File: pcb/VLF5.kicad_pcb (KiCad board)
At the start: 6 copper layers, 34 x 56 mm, 92 parts, among them CN1 532610571, J1 Conn_01x02_Pin, Q1 SS8050, Q3 SS8050, Q4 SS8050, Q5 SI7232DN-T1-GE3, U1 STM32H743VIHx, U10 LSM6DSMTR, U11 LIS2MDL, U15 ISO1044BD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

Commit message: ufl
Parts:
- added R14: 0R, Resistor_SMD:R_0603_1608Metric, B.Cu at (91.4, 7.57)
- added U8: BWU.FL-IPEX1, Rocketry_Easyeda:IPEX-SMD_BWIPX-1-001E, B.Cu at (83.5, 9.34)
- moved U6 1.65 mm to (83.7, 2.13)

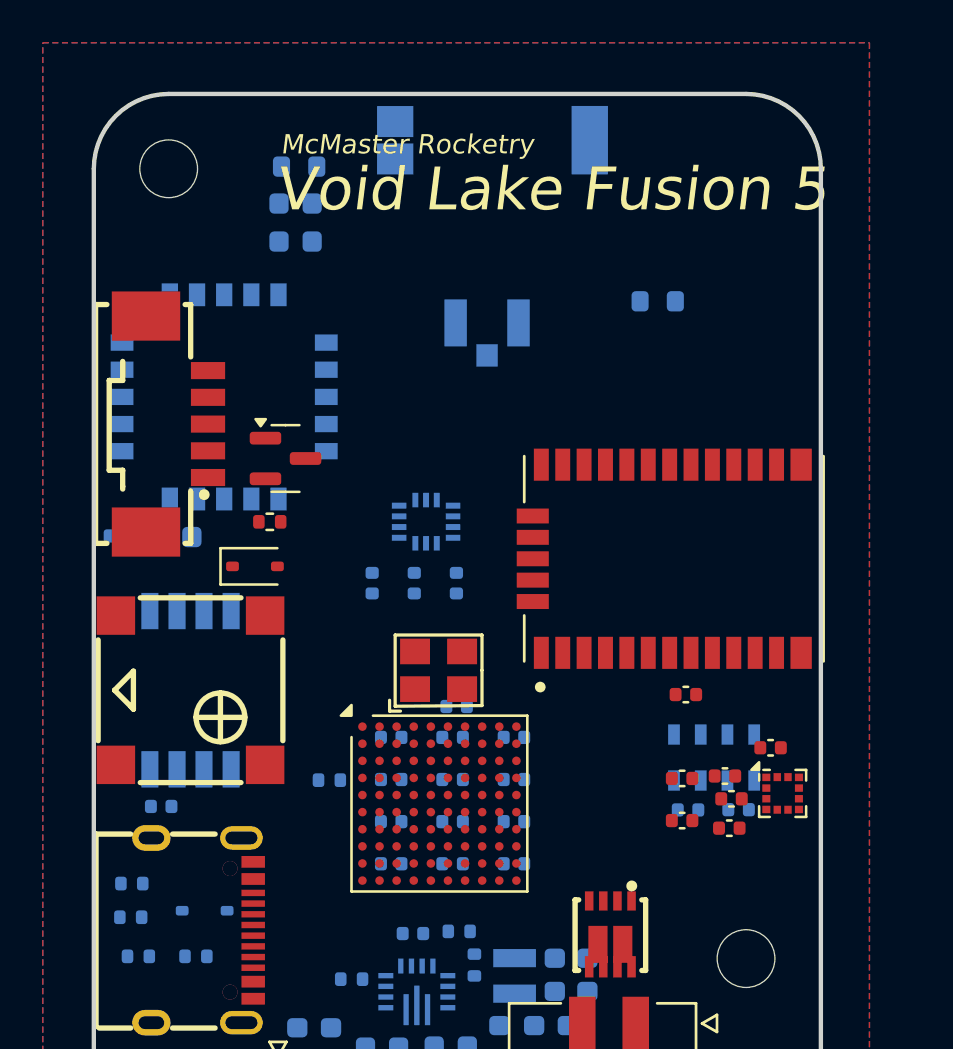
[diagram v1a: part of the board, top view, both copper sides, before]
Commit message: added active gps antenna connector
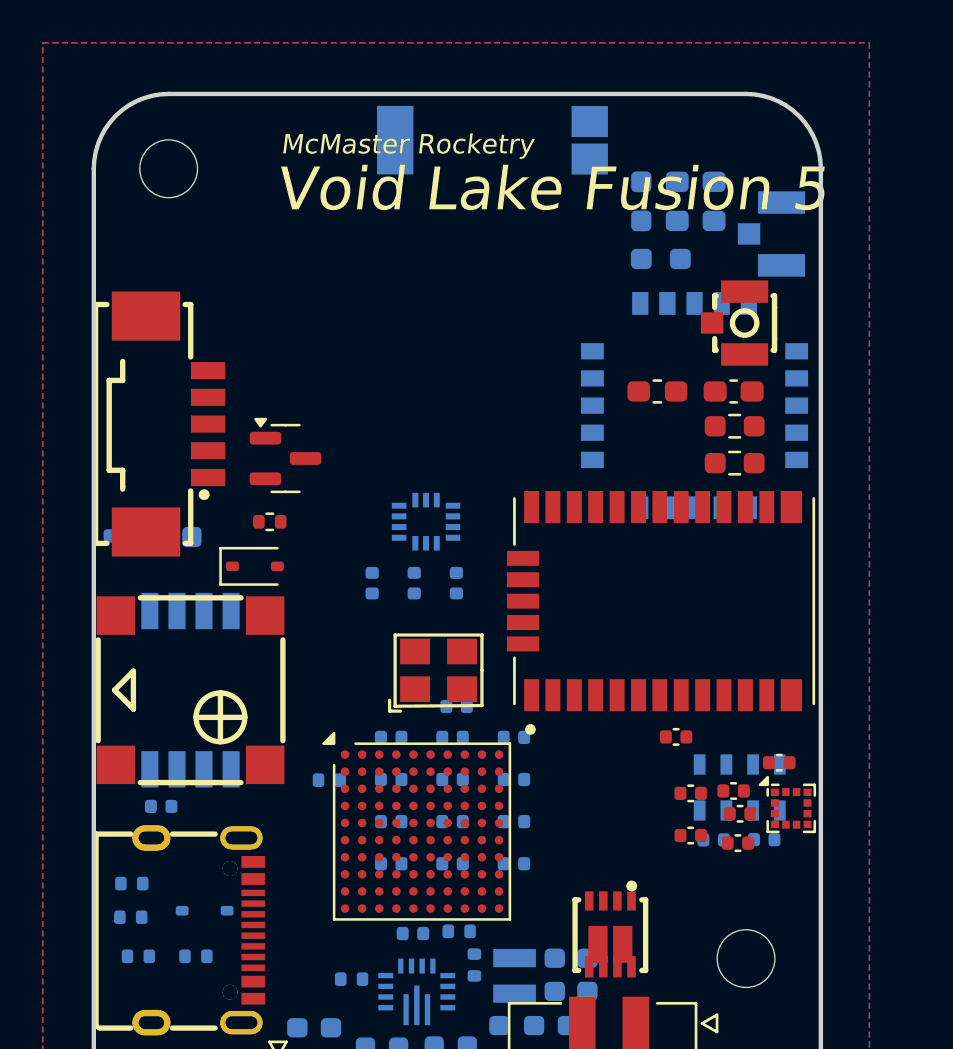
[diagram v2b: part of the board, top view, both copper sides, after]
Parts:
- added C13: 47pF, Capacitor_SMD:C_0603_1608Metric_Pad1.08x0.95mm_HandSolder, F.Cu at (95.0, 11.8)
- added L3: 27nH, Inductor_SMD:L_0603_1608Metric_Pad1.05x0.95mm_HandSolder, F.Cu at (91.4, 11.8)
- added R16: 0R, Resistor_SMD:R_0603_1608Metric_Pad0.98x0.95mm_HandSolder, F.Cu at (95.0, 13.4)
- added R17: 0R, Resistor_SMD:R_0603_1608Metric_Pad0.98x0.95mm_HandSolder, F.Cu at (95.0, 15.1)
- added U12: BWU.FL-IPEX1, Rocketry_Easyeda:IPEX-SMD_BWIPX-1-001E, F.Cu at (94.8, 8.59)
- C28, C46: footprint Capacitor_SMD:C_0603_1608Metric -> Capacitor_SMD:C_0603_1608Metric_Pad1.08x0.95mm_HandSolder
- R14, R31: footprint Resistor_SMD:R_0603_1608Metric -> Resistor_SMD:R_0603_1608Metric_Pad0.98x0.95mm_HandSolder
- U6: footprint Rocketry_Manual:W3012-ANT-PKG-Mirrored -> Rocketry_Manual:W3012-ANT-PKG
- moved U7 22.0 mm to (93.2, 12.4)
- moved C46 18.9 mm to (93.2, 1.98), turned to 0 degrees
- moved C28 18.7 mm to (93.2, 3.81), turned to 0 degrees
- moved R31 16.1 mm to (90.7, 2.90), turned to -90 degrees
- moved U8 13.9 mm to (96.5, 4.42), turned to 0 degrees
- moved C27 2.03 mm to (92.3, 27.9)
- moved U5 2.03 mm to (91.7, 21.6)
- moved R14 1.99 mm to (91.6, 5.59)
- moved C12 1.84 mm to (96.4, 32.7)
- moved U9 1.84 mm to (95.3, 30.3)
- moved C11 1.84 mm to (94.1, 32.8)
- moved U1 1.54 mm to (80.4, 32.4)
- moved C22 0.81 mm to (95.0, 30.5)
- moved C23 0.81 mm to (95.3, 31.5)
- moved C24 0.81 mm to (95.2, 32.9)
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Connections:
- C23 pad 2: +3.3VA -> +3.3V
- C24 pad 2: +3.3VA -> +3.3V
- C41 pad 2: +3.3VA -> +3.3V
- R14 pad 2: Net-(U6-ANT) -> Net-(U7-ANT)
- U11 pad 10: +3.3VA -> +3.3V
- U5 pad 16: Net-(U5-RF_IN) -> Net-(U5-RF_OUT)

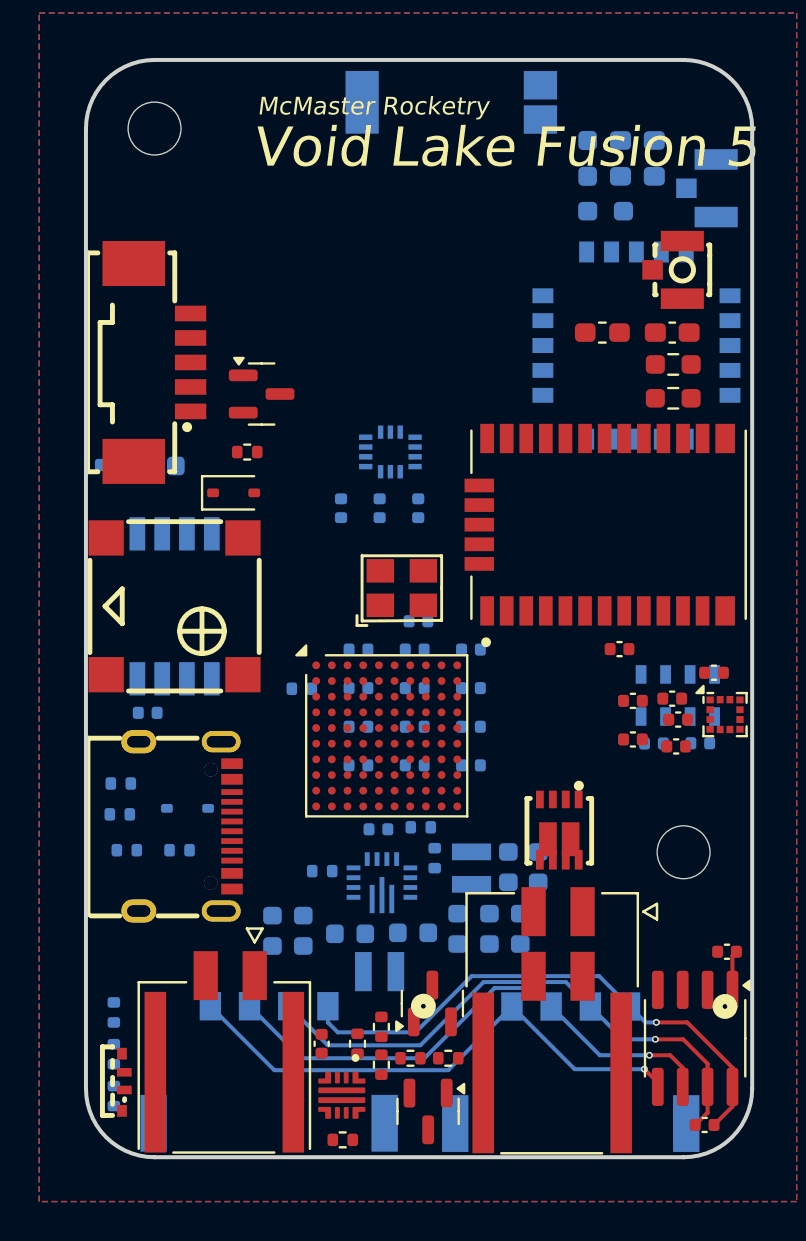
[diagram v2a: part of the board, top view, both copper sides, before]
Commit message: add pull up resistor for sd, change pad net
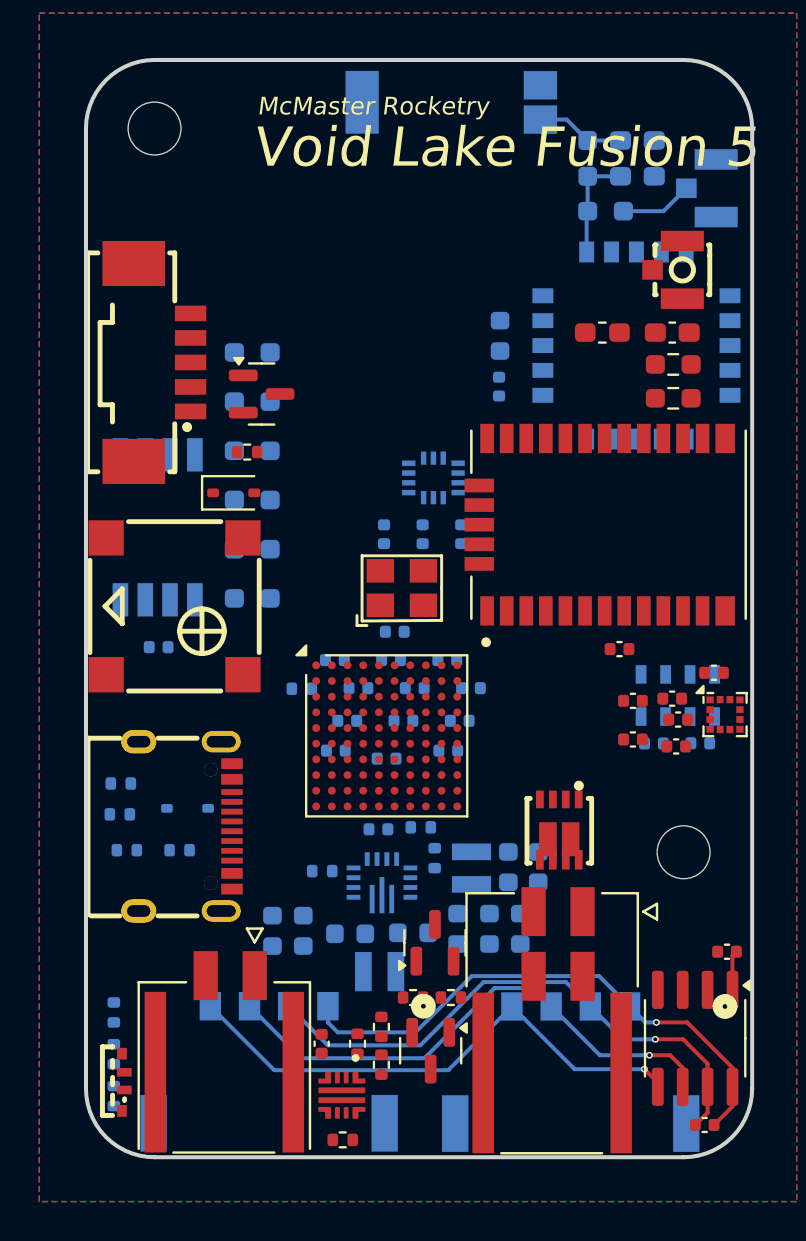
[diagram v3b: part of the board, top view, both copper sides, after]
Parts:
- added R15: 10K, Resistor_SMD:R_0603_1608Metric_Pad0.98x0.95mm_HandSolder, B.Cu at (73.6, 12.8)
- added R18: 10K, Resistor_SMD:R_0603_1608Metric_Pad0.98x0.95mm_HandSolder, B.Cu at (73.6, 15.3)
- added R19: 10K, Resistor_SMD:R_0603_1608Metric_Pad0.98x0.95mm_HandSolder, B.Cu at (73.6, 17.8)
- added R20: 10K, Resistor_SMD:R_0603_1608Metric_Pad0.98x0.95mm_HandSolder, B.Cu at (73.6, 20.3)
- added R21: 10K, Resistor_SMD:R_0603_1608Metric_Pad0.98x0.95mm_HandSolder, B.Cu at (73.6, 22.8)
- added R23: 10K, Resistor_SMD:R_0603_1608Metric_Pad0.98x0.95mm_HandSolder, B.Cu at (73.6, 25.3)
- moved C25 20.3 mm to (86.2, 14.5), turned to -90 degrees
- moved C26 18.6 mm to (86.2, 12.0), turned to -90 degrees
- moved U2 4.12 mm to (68.7, 21.7)
- moved C20 3.40 mm to (68.8, 27.8)
- moved R10 3.10 mm to (81.8, 45.7)
- moved Q3 3.10 mm to (82.7, 48.4)
- moved R9 3.10 mm to (83.7, 45.7)
- moved Q1 3.10 mm to (82.9, 42.9)
- moved C16 2.57 mm to (84.2, 22.1)
- moved C17 2.57 mm to (82.3, 22.1)
- moved C18 2.57 mm to (80.3, 22.1)
- moved U10 2.57 mm to (82.8, 19.2)
- moved C36 1.48 mm to (80.4, 33.5)
- moved C40 1.38 mm to (77.8, 33.1)
- moved C32 1.38 mm to (83.6, 33.1)
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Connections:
- net /Peripherals/IMU_INT1 renamed /IMU_INT1
- net /Peripherals/IMU_INT2 renamed /IMU_INT2
- net /Pyro/PYRO1_CONT renamed /PYRO1_CONT
- net /Pyro/PYRO2_CONT renamed /PYRO2_CONT
- net /RF/GPS_PPS renamed /GPS_PPS
- J1 pad S2: (no net) -> +BATT
- J_PYRO1 pad S1: (no net) -> Net-(J_PYRO1-Pin_3)
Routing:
- net Net-(U7-ANT): track 0.00 -> 5.56 mm
- net Net-(U6-ANT): track 0.00 -> 4.53 mm
- net Net-(R14-Pad1): track 0.00 -> 3.70 mm

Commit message: Original Layout with Pins Configured
🙏
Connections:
- D1 pad 2: /Power/VBUS -> /VBUS
- J1 pad S2: +BATT -> (no net)
- J_PYRO1 pad S1: Net-(J_PYRO1-Pin_3) -> (no net)
- Q5 pad 2: /Pyro/PYRO1_CTRL -> /PYRO1_CTRL
- Q5 pad 4: /Pyro/PYRO2_CTRL -> /PYRO2_CTRL
- R11 pad 1: /Power/BAT_V_M -> /BAT_V_M
- R12 pad 2: /Power/BAT_V_M -> /BAT_V_M
- R13 pad 2: /Peripherals/BUZZER_CTRL -> /BUZZER_CTRL
- R15 pad 1: /Peripherals/SD_DAT2 -> /SD_DAT2
- R18 pad 1: /Peripherals/SD_DAT3 -> /SD_DAT3
- R19 pad 1: /Peripherals/SD_CLK -> /SD_CLK
- R20 pad 1: /Peripherals/SD_DAT1 -> /SD_DAT1
- R21 pad 1: /Peripherals/SD_DAT0 -> /SD_DAT0
- R23 pad 1: /Peripherals/SD_CMD -> /SD_CMD
- R24 pad 1: /Peripherals/LED_B_CTRL -> /LED_B_CTRL
- R25 pad 1: /Peripherals/LED_G_CTRL -> /LED_G_CTRL
- R26 pad 1: /Peripherals/LED_R_CTRL -> /LED_R_CTRL
- R8 pad 2: /Pyro/PYRO_nEN -> /PYRO_nEN
- U1 pad A1: unconnected-(U1-PC14-PadA1) -> /IMU_INT1
- U1 pad A2: unconnected-(U1-PC13-PadA2) -> /IMU_CS
- U1 pad A3: unconnected-(U1-PE2-PadA3) -> /IMU_CLK
- U1 pad A4: unconnected-(U1-PB9-PadA4) -> /IMU_INT2
- U1 pad A5: unconnected-(U1-PB7-PadA5) -> /MAG_SDA
- U1 pad A6: unconnected-(U1-PB4-PadA6) -> /LORA_MISO
- U1 pad A7: unconnected-(U1-PB3-PadA7) -> /LORA_SCK
- U1 pad A8: unconnected-(U1-PA15-PadA8) -> /GPS_PPS
- U1 pad B1: unconnected-(U1-PC15-PadB1) -> /BUZZER_CTRL
- U1 pad B10: unconnected-(U1-PA12-PadB10) -> /DP
- U1 pad B4: unconnected-(U1-PB8-PadB4) -> /MAG_SCL
- U1 pad B5: unconnected-(U1-PB6-PadB5) -> /GPS_TX
- U1 pad B6: unconnected-(U1-PD5-PadB6) -> /LORA_nRST
- U1 pad B7: unconnected-(U1-PD2-PadB7) -> /SD_CMD
- U1 pad B8: unconnected-(U1-PC11-PadB8) -> /SD_DAT3
- U1 pad B9: unconnected-(U1-PC10-PadB9) -> /SD_DAT2
- U1 pad C10: unconnected-(U1-PA11-PadC10) -> /DN
- U1 pad C5: unconnected-(U1-PB5-PadC5) -> /BARO_MOSI
- U1 pad C6: unconnected-(U1-PD6-PadC6) -> /LORA_MOSI
- U1 pad C7: unconnected-(U1-PD3-PadC7) -> /LORA_BUSY
- U1 pad C8: unconnected-(U1-PC12-PadC8) -> /SD_CLK
- U1 pad C9: unconnected-(U1-PA9-PadC9) -> /VBUS
- U1 pad D10: unconnected-(U1-PA10-PadD10) -> /GPS_RX
- U1 pad D3: unconnected-(U1-PE5-PadD3) -> /IMU_MISO
- U1 pad D7: unconnected-(U1-PD4-PadD7) -> /LORA_CS
- U1 pad D8: unconnected-(U1-PD0-PadD8) -> /LORA_RXEN
- U1 pad D9: unconnected-(U1-PA8-PadD9) -> /LORA_DIO1
- U1 pad E10: unconnected-(U1-PC7-PadE10) -> /GPS_nRST
- U1 pad E3: unconnected-(U1-PE6-PadE3) -> /IMU_MOSI
- U1 pad E8: unconnected-(U1-PD1-PadE8) -> /LORA_TXEN
- U1 pad E9: unconnected-(U1-PC9-PadE9) -> /SD_DAT1
- U1 pad F10: unconnected-(U1-PC6-PadF10) -> /BARO_CS
- U1 pad F9: unconnected-(U1-PC8-PadF9) -> /SD_DAT0
- U1 pad G9: unconnected-(U1-PD11-PadG9) -> /PYRO_nEN
- U1 pad H3: unconnected-(U1-PA5-PadH3) -> /BARO_CLK
- U1 pad H9: unconnected-(U1-PD10-PadH9) -> /PYRO_PG
- U1 pad J10: unconnected-(U1-PD13-PadJ10) -> /PYRO1_CONT
- U1 pad J3: unconnected-(U1-PA6-PadJ3) -> /BARO_MISO
- U1 pad J4: unconnected-(U1-PB0-PadJ4) -> /BAT_V_M
- U1 pad J8: unconnected-(U1-PB13-PadJ8) -> /CAN_TX
- U1 pad J9: unconnected-(U1-PD9-PadJ9) -> /PYRO2_CTRL
- U1 pad K10: unconnected-(U1-PD12-PadK10) -> /PYRO2_CONT
- U1 pad K2: unconnected-(U1-PA3-PadK2) -> /LED_R_CTRL
- U1 pad K3: unconnected-(U1-PA7-PadK3) -> /LED_G_CTRL
- U1 pad K4: unconnected-(U1-PB1-PadK4) -> /LED_B_CTRL
- U1 pad K6: unconnected-(U1-PE13-PadK6) -> /PS
- U1 pad K8: unconnected-(U1-PB12-PadK8) -> /CAN_RX
- U1 pad K9: unconnected-(U1-PD8-PadK9) -> /PYRO1_CTRL
- U10 pad 1: /Peripherals/IMU_MISO -> /IMU_MISO
- U10 pad 12: /Peripherals/IMU_CS -> /IMU_CS
- U10 pad 13: /Peripherals/IMU_CLK -> /IMU_CLK
- U10 pad 14: /Peripherals/IMU_MOSI -> /IMU_MOSI
- U11 pad 1: /Peripherals/MAG_SCL -> /MAG_SCL
- U11 pad 4: /Peripherals/MAG_SDA -> /MAG_SDA
- U15 pad 2: /Peripherals/CAN_TX -> /CAN_TX
- U15 pad 3: /Peripherals/CAN_RX -> /CAN_RX
- U2 pad 1: /Peripherals/SD_DAT2 -> /SD_DAT2
- U2 pad 2: /Peripherals/SD_DAT3 -> /SD_DAT3
- U2 pad 3: /Peripherals/SD_CLK -> /SD_CLK
- U2 pad 5: /Peripherals/SD_CMD -> /SD_CMD
- U2 pad 6: /Peripherals/SD_DAT0 -> /SD_DAT0
- U2 pad 7: /Peripherals/SD_DAT1 -> /SD_DAT1
- U3 pad 2: /Pyro/PYRO_nEN -> /PYRO_nEN
- U3 pad 3: /Pyro/PYRO_PG -> /PYRO_PG
- U4 pad 1: /Power/PS -> /PS
- U5 pad 23: /RF/GPS_nRST -> /GPS_nRST
- U5 pad 25: /RF/GPS_TX -> /GPS_TX
- U5 pad 26: /RF/GPS_RX -> /GPS_RX
- U7 pad 10: /RF/LORA_RXEN -> /LORA_RXEN
- U7 pad 11: /RF/LORA_BUSY -> /LORA_BUSY
- U7 pad 12: /RF/LORA_MISO -> /LORA_MISO
- U7 pad 13: /RF/LORA_MOSI -> /LORA_MOSI
- U7 pad 14: /RF/LORA_CS -> /LORA_CS
- U7 pad 15: /RF/LORA_SCK -> /LORA_SCK
- U7 pad 20: /RF/LORA_DIO1 -> /LORA_DIO1
- U7 pad 3: /RF/LORA_nRST -> /LORA_nRST
- U7 pad 9: /RF/LORA_TXEN -> /LORA_TXEN
- U9 pad 4: /Peripherals/BARO_CS -> /BARO_CS
- U9 pad 5: /Peripherals/BARO_CS -> /BARO_CS
- U9 pad 6: /Peripherals/BARO_MISO -> /BARO_MISO
- U9 pad 7: /Peripherals/BARO_MOSI -> /BARO_MOSI
- U9 pad 8: /Peripherals/BARO_CLK -> /BARO_CLK
- USB1 pad 11: /Power/VBUS -> /VBUS
- USB1 pad 2: /Power/VBUS -> /VBUS
- USB1 pad 5: /Power/DN -> /DN
- USB1 pad 6: /Power/DP -> /DP
- USB1 pad 7: /Power/DN -> /DN
- USB1 pad 8: /Power/DP -> /DP
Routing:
- added copper zone on B.Cu, net +3.3V
- added copper zone on B.Cu, net +BATT

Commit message: Playing with configs Template
As title describes
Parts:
- moved C44 77.4 mm to (116.1, 96.0)
- moved C33 77.1 mm to (116.1, 97.0)
- moved RBOOT1 76.8 mm to (109.5, 99.1), turned to -90 degrees
- moved C37 76.5 mm to (114.1, 95.8)
- moved C36 75.7 mm to (116.2, 100.3)
- moved C38 75.7 mm to (114.1, 97.0)
- moved C39 75.5 mm to (114.0, 98.1)
- moved C40 75.3 mm to (114.1, 99.2)
- moved C34 74.1 mm to (108.4, 99.1), turned to -90 degrees
- moved C31 73.8 mm to (116.2, 98.1)
- moved C32 73.7 mm to (116.3, 99.2)
- moved C35 73.6 mm to (110.5, 99.1), turned to -90 degrees
- moved Q5 61.0 mm to (82.7, 97.8)
- moved Q1 57.0 mm to (77.9, 99.7)
- moved R10 55.1 mm to (81.8, 100.8)
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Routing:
- net Net-(J_CAN1-Pin_2): track 28.7 -> 0.00 mm, vias 1 -> 0
- net Net-(J_CAN1-Pin_1): track 28.1 -> 0.00 mm, vias 1 -> 0
- net Net-(J_CAN1-Pin_4): track 27.4 -> 0.00 mm, vias 1 -> 0
- net Net-(J_CAN1-Pin_3): track 27.4 -> 0.00 mm, vias 1 -> 0
- net /LORA_RXEN: track 0.00 -> 20.6 mm
- net /LORA_TXEN: track 0.00 -> 19.9 mm
- net /LORA_BUSY: track 0.00 -> 15.3 mm
- net /LORA_MISO: track 0.00 -> 14.5 mm
- net /LORA_MOSI: track 0.00 -> 13.6 mm
- net /nRST: track 0.00 -> 12.0 mm
- net /LORA_CS: track 0.00 -> 11.0 mm
- net /LORA_nRST: track 0.00 -> 10.8 mm
- net /GPS_nRST: track 0.00 -> 9.69 mm
- net /LORA_SCK: track 0.00 -> 9.66 mm
- net /SWDCLK: track 0.00 -> 8.47 mm
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- added copper zone on B.Cu, net Net-(U4-L1)
- added copper zone on B.Cu, net Net-(U4-L2)

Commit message: Iterating
Iterating
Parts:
- C29, C30, C36, C39, C44: moved to F.Cu
- moved C44 60.2 mm to (64.6, 64.8), turned to -90 degrees
- moved C36 59.0 mm to (66.0, 69.2), turned to 0 degrees
- moved C39 58.6 mm to (64.6, 66.7), turned to 90 degrees
- moved U1 47.3 mm to (70.1, 63.7)
- moved C29 45.8 mm to (64.1, 59.9), turned to 0 degrees
- moved X1 45.5 mm to (63.6, 62.1)
- moved C30 45.4 mm to (63.0, 64.4), turned to 0 degrees
- moved C32 34.1 mm to (108.9, 65.9)
- moved C34 33.1 mm to (112.6, 66.3), turned to 90 degrees
- moved C40 32.2 mm to (109.3, 67.3), turned to -90 degrees
- moved RBOOT1 31.9 mm to (116.4, 67.9), turned to 90 degrees
- moved C35 31.0 mm to (113.6, 68.3), turned to 90 degrees
- moved C33 30.6 mm to (110.4, 66.9), turned to -90 degrees
- moved C31 29.8 mm to (110.4, 68.8), turned to 90 degrees
- moved C38 28.8 mm to (112.6, 68.2), turned to 90 degrees
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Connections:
- U1 pad B5: /GPS_TX -> /CAN_TX
- U1 pad C5: /BARO_MOSI -> /CAN_RX
- U1 pad D6: unconnected-(U1-PD7-PadD6) -> /BARO_MOSI
- U1 pad H10: unconnected-(U1-PB14-PadH10) -> /GPS_TX
- U1 pad J8: /CAN_TX -> unconnected-(U1-PB13-PadJ8)
- U1 pad K8: /CAN_RX -> unconnected-(U1-PB12-PadK8)
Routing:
- net /LORA_RXEN: track 20.6 -> 13.5 mm
- net GND: track 0.00 -> 6.58 mm
- net Net-(U1-PH1): track 0.00 -> 5.89 mm
- net /Pyro/PYRO2: track 0.00 -> 5.71 mm
- net /Pyro/PYRO1: track 0.00 -> 5.70 mm
- net /LORA_TXEN: track 19.9 -> 14.3 mm
- net +3.3V: track 0.00 -> 4.88 mm
- net /PYRO_PG: track 0.00 -> 4.17 mm
- net +3.3VA: track 0.00 -> 4.12 mm
- net Net-(U1-PH0): track 0.00 -> 3.37 mm
- net /PYRO1_CONT: track 0.00 -> 2.84 mm
- net /PYRO2_CONT: track 0.00 -> 2.66 mm
- net Net-(Q3-B): track 0.00 -> 1.84 mm
- net Net-(Q1-B): track 0.00 -> 1.84 mm
- net /LORA_nRST: track 10.8 -> 12.6 mm
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
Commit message: Changed Pins new Layout
Changed Pins new Layout
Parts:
- moved C43 48.8 mm to (79.7, 65.2), turned to 180 degrees
- moved U11 47.4 mm to (80.9, 63.3)
- moved C41 47.2 mm to (82.6, 61.1), turned to -90 degrees
- moved C42 47.0 mm to (81.6, 65.2)
- moved C24 44.9 mm to (80.7, 61.1), turned to -90 degrees
- moved C23 44.1 mm to (81.6, 61.1), turned to -90 degrees
- moved C22 43.5 mm to (82.6, 63.4), turned to 90 degrees
- moved C11 37.1 mm to (83.6, 66.2)
- moved C12 37.1 mm to (83.6, 67.2)
- moved U9 37.1 mm to (82.2, 63.8)
- moved U10 30.1 mm to (69.1, 52.5)
- moved C16 30.1 mm to (72.4, 51.1)
- moved C17 30.1 mm to (71.4, 51.1)
- moved C18 30.1 mm to (69.0, 50.5)
- moved C20 15.1 mm to (53.4, 58.2)
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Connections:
- U1 pad A5: /MAG_SDA -> unconnected-(U1-PB7-PadA5)
- U1 pad B4: /MAG_SCL -> unconnected-(U1-PB8-PadB4)
- U1 pad J7: unconnected-(U1-PB10-PadJ7) -> /MAG_SCL
- U1 pad K7: unconnected-(U1-PB11-PadK7) -> /MAG_SDA
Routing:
- net +3.3V: track 4.88 -> 9.38 mm, vias 0 -> 4
- net Net-(U3-EN/UVLO): track 0.00 -> 3.46 mm
- net +BATT: track 0.00 -> 2.13 mm, vias 0 -> 1
- net /MAG_SDA: track 4.23 -> 2.16 mm
- net Net-(U11-C1): track 0.00 -> 2.00 mm
- net GND: track 6.58 -> 8.37 mm, vias 0 -> 4
- net /MAG_SCL: track 3.56 -> 1.91 mm
- net unconnected-(U1-PB12-PadK8): track 0.90 -> 0.00 mm
- net /BARO_CS: track 3.89 -> 4.79 mm
- net +3.3VA: vias 0 -> 2
